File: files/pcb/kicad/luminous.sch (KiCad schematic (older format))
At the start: 0 parts

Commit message: 回路図更新
温度湿度センサ
大気圧センサ
輝度センサ
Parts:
- added PD: DIODE, ~, symbol DIODE
- added R?: 10k, ~, symbol R
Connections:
- new net +5V: PD.1 (A)
- new net GND: R?.1
- new net out: PD.2 (K), R?.2
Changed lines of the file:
@@
 $Descr A4 11693 8268
 encoding utf-8
-Sheet 1 12
+Sheet 3 12
 Title ""
 Date "23 aug 2014"
@@
 Comment4 ""
 $EndDescr
+Text HLabel 5950 3750 2    60   Input ~ 0
+out
+$Comp
+L DIODE PD
+U 1 1 53F8E30F
+P 5700 3450
+F 0 "PD" H 5700 3550 40  0000 C CNN
+F 1 "DIODE" H 5700 3350 40  0000 C CNN
+F 2 "~" H 5700 3450 60  0000 C CNN
+F 3 "~" H 5700 3450 60  0000 C CNN
+	1    5700 3450
+	0    1    1    0
+$EndComp
+$Comp
+L R R?
+U 1 1 53F8E31E
+P 5700 4100
+F 0 "R?" V 5780 4100 40  0000 C CNN
+F 1 "10k" V 5707 4101 40  0000 C CNN
+F 2 "~" V 5630 4100 30  0000 C CNN
+F 3 "~" H 5700 4100 30  0000 C CNN
+	1    5700 4100
+	-1   0    0    1
+$EndComp
+$Comp
+L GND #PWR?
+U 1 1 53F8E33E
+P 5700 4450
+F 0 "#PWR?" H 5700 4450 30  0001 C CNN
+F 1 "GND" H 5700 4380 30  0001 C CNN
+F 2 "" H 5700 4450 60  0000 C CNN
+F 3 "" H 5700 4450 60  0000 C CNN
+	1    5700 4450
+	1    0    0    -1
+$EndComp
+$Comp
+L +5V #PWR?
+U 1 1 53F8E34D
+P 5700 3150
+F 0 "#PWR?" H 5700 3240 20  0001 C CNN
+F 1 "+5V" H 5700 3240 30  0000 C CNN
+F 2 "" H 5700 3150 60  0000 C CNN
+F 3 "" H 5700 3150 60  0000 C CNN
+	1    5700 3150
+	1    0    0    -1
+$EndComp
+Wire Wire Line
+	5700 3250 5700 3150
+Wire Wire Line
+	5700 3650 5700 3850
+Wire Wire Line
+	5700 4350 5700 4450
+Wire Wire Line
+	5950 3750 5700 3750
+Connection ~ 5700 3750
 $EndSCHEMATC

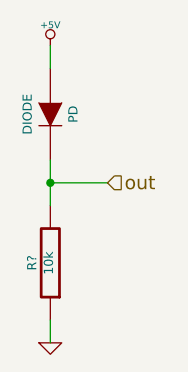
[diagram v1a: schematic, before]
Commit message: 回路図更新、DS1307対応
バスの接続が未
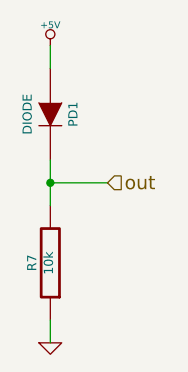
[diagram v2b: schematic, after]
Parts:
- gave numbers to parts that had none: 1
- renumbered PD to PD1
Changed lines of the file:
@@
 $Descr A4 11693 8268
 encoding utf-8
-Sheet 3 12
+Sheet 4 13
 Title ""
-Date "23 aug 2014"
+Date "24 aug 2014"
 Rev ""
 Comp ""
@@
 out
 $Comp
-L DIODE PD
+L DIODE PD1
 U 1 1 53F8E30F
 P 5700 3450
-F 0 "PD" H 5700 3550 40  0000 C CNN
+F 0 "PD1" H 5700 3550 40  0000 C CNN
 F 1 "DIODE" H 5700 3350 40  0000 C CNN
 F 2 "~" H 5700 3450 60  0000 C CNN
@@
 $EndComp
 $Comp
-L R R?
+L R R7
 U 1 1 53F8E31E
 P 5700 4100
-F 0 "R?" V 5780 4100 40  0000 C CNN
+F 0 "R7" V 5780 4100 40  0000 C CNN
 F 1 "10k" V 5707 4101 40  0000 C CNN
 F 2 "~" V 5630 4100 30  0000 C CNN
@@
 $EndComp
 $Comp
-L GND #PWR?
+L GND #PWR24
 U 1 1 53F8E33E
 P 5700 4450
-F 0 "#PWR?" H 5700 4450 30  0001 C CNN
+F 0 "#PWR24" H 5700 4450 30  0001 C CNN
 F 1 "GND" H 5700 4380 30  0001 C CNN
 F 2 "" H 5700 4450 60  0000 C CNN
@@
 $EndComp
 $Comp
-L +5V #PWR?
+L +5V #PWR23
 U 1 1 53F8E34D
 P 5700 3150
-F 0 "#PWR?" H 5700 3240 20  0001 C CNN
+F 0 "#PWR23" H 5700 3240 20  0001 C CNN
 F 1 "+5V" H 5700 3240 30  0000 C CNN
 F 2 "" H 5700 3150 60  0000 C CNN

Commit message: 回路図ERC途中
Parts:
- PD1: value DIODE -> PHOTO_DIODE
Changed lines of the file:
@@
 Sheet 4 13
 Title ""
-Date "24 aug 2014"
+Date "25 aug 2014"
 Rev ""
 Comp ""
@@
 P 5700 3450
 F 0 "PD1" H 5700 3550 40  0000 C CNN
-F 1 "DIODE" H 5700 3350 40  0000 C CNN
+F 1 "PHOTO_DIODE" H 5700 3350 40  0000 C CNN
 F 2 "~" H 5700 3450 60  0000 C CNN
 F 3 "~" H 5700 3450 60  0000 C CNN
@@
 $EndComp
 $Comp
-L GND #PWR24
+L GND #PWR024
 U 1 1 53F8E33E
 P 5700 4450
-F 0 "#PWR24" H 5700 4450 30  0001 C CNN
+F 0 "#PWR024" H 5700 4450 30  0001 C CNN
 F 1 "GND" H 5700 4380 30  0001 C CNN
 F 2 "" H 5700 4450 60  0000 C CNN
@@
 $EndComp
 $Comp
-L +5V #PWR23
+L +5V #PWR025
 U 1 1 53F8E34D
 P 5700 3150
-F 0 "#PWR23" H 5700 3240 20  0001 C CNN
+F 0 "#PWR025" H 5700 3240 20  0001 C CNN
 F 1 "+5V" H 5700 3240 30  0000 C CNN
 F 2 "" H 5700 3150 60  0000 C CNN

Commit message: 部品リスト・パッケージライブラリを更新
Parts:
- renumbered R7 to R11
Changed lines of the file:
@@
 $EndComp
 $Comp
-L R R7
+L R R11
 U 1 1 53F8E31E
 P 5700 4100
-F 0 "R7" V 5780 4100 40  0000 C CNN
+F 0 "R11" V 5780 4100 40  0000 C CNN
 F 1 "10k" V 5707 4101 40  0000 C CNN
 F 2 "~" V 5630 4100 30  0000 C CNN
